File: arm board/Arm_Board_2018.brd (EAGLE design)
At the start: 100.3 x 64.8 mm, 190 parts, among them J1 RJ45KEYSTONE-942, J10 APP_2POS_CONFIGGENERAL_CONFIG, J11 APP_2POS_CONFIGGENERAL_CONFIG, J12 APP_2POS_CONFIGGENERAL_CONFIG, J13 APP_2POS_CONFIGGENERAL_CONFIG, J14 SL02, J15 SL02, J16 SL02, J2 JTAG_ARM_10PIN, J4 SL02, J5 APP_2POS_CONFIGGENERAL_CONFIG, J6 APP_2POS_CONFIGGENERAL_CONFIG, J7 APP_2POS_CONFIGGENERAL_CONFIG, J9 APP_2POS_CONFIGGENERAL_CONFIG, Q1 Q_IRF7437SMD, U1 TM4C1294NCPDT, U2 HX1198FNL, U3 SLVU2.8-4, Y1 NX3225GA, Y2 CRYATL_32K_SMD

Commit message: Switched wires to nets, corrected couple of naming errors
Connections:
- removed net MOTOR23_CURRENT_SENSOR: U$21.3
- removed net N$52: C44.1, C45.1, C46.1, C47.1
- removed net N$82: R61.1, R62.1, R63.1, R64.1, R65.1, R66.1
- removed net N$85: R55.2
- removed net N$86: R54.2
- net GND: now also C44.1, C45.1, C46.1, C47.1, R54.2, R55.2, R61.1, R62.1, R63.1, R64.1, R65.1, R66.1
- net MOTOR3_CURRENT_SENSOR: now also U$21.3

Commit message: Fixed remaining SCH issues, warnings, and missing parts
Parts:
- removed C50: 2.2uF, SparkFun-Passives:0603-CAP
- added C61, C63, C64, C65, C66, C67, C68: .1uF, SparkFun-Passives:0603-CAP
- added C62: 1nF, SparkFun-Passives:0603-CAP
- added C69, C70, C71, C72, C73, C74: 1uF, SparkFun-Passives:0603-CAP
- added C75: 2.2uF, SparkFun-Capacitors:1206
- added R59, R60, R67, R68, R69, R70: 1k, SparkFun-Passives:0402-RES
- C48, C49, C54: value (none) -> .1uF
- C51: device SparkFun-Passives:0603-CAP -> SparkFun-Capacitors:1206
- C53: value (none) -> 10uF
- moved C52 1187.1 mm to (64.8, -22.9)
- moved C53 1187.1 mm to (64.8, -52.1)
- moved C55 1187.1 mm to (64.8, -54.6)
- moved C56 1187.1 mm to (64.8, -57.1)
- moved C57 1187.1 mm to (64.8, -59.7)
- moved C58 1187.1 mm to (64.8, -62.2)
- moved C59 1187.1 mm to (64.8, -64.8)
- moved C60 1187.1 mm to (64.8, -67.3)
- moved POWER_12V 1187.1 mm to (132.1, 57.1)
- moved Q1 1187.1 mm to (74.9, -39.4)
- moved R51 1187.1 mm to (124.5, -19.1)
- moved R52 1187.1 mm to (120.7, -19.1)
- moved R53 1187.1 mm to (116.8, -19.1)
- moved R54 1187.1 mm to (113.0, -19.1)
- moved R55 1187.1 mm to (109.2, -19.1)
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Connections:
- new net N$12: R59.1, U$24.3
- new net N$13: R60.1, U$25.3
- new net N$20: R67.1, U$23.3
- new net N$32: R68.1, U$21.3
- new net N$38: R69.1, U$22.3
- new net N$44: R70.1, U$20.3
- net GND: now also C51.1, C61.2, C62.1, C63.1, C64.1, C65.1, C66.1, C67.1, C68.1, C69.2, C70.2, C71.1, C72.1, C73.1, C74.1, C75.2; no longer C50.2, C51.2
- net LOGIC_3.3V: now also C61.1, C63.2, C64.2, C65.2, C66.2, C67.2, C68.2, C75.1; no longer C50.1
- net MAINLINE_CURRENT_SENSOR: now also C62.2
- net MOTOR1_CURRENT_SENSOR: now also C74.2, R70.2; no longer U$20.3
- net MOTOR2_CURRENT_SENSOR: now also C73.2, R69.2; no longer U$22.3
- net MOTOR3_CURRENT_SENSOR: now also C72.2, R68.2; no longer U$21.3
- net MOTOR4_CURRENT_SENSOR: now also C71.2, R67.2; no longer U$23.3
- net MOTOR5_CURRENT_SENSOR: now also C69.1, R59.2; no longer U$24.3
- net MOTOR6_CURRENT_SENSOR: now also C70.1, R60.2; no longer U$25.3
- net VCC_12V: now also C51.2; no longer C51.1
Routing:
- net !RESET: track 80.8 -> 70.4 mm
- removed copper zone on layer 1, net +12V_ACT
- removed copper zone on layer 1, net +12V_LOGIC
- removed copper zone on layer 1, net +5V_ACT
- removed copper zone on layer 1, net +5V_LOGIC

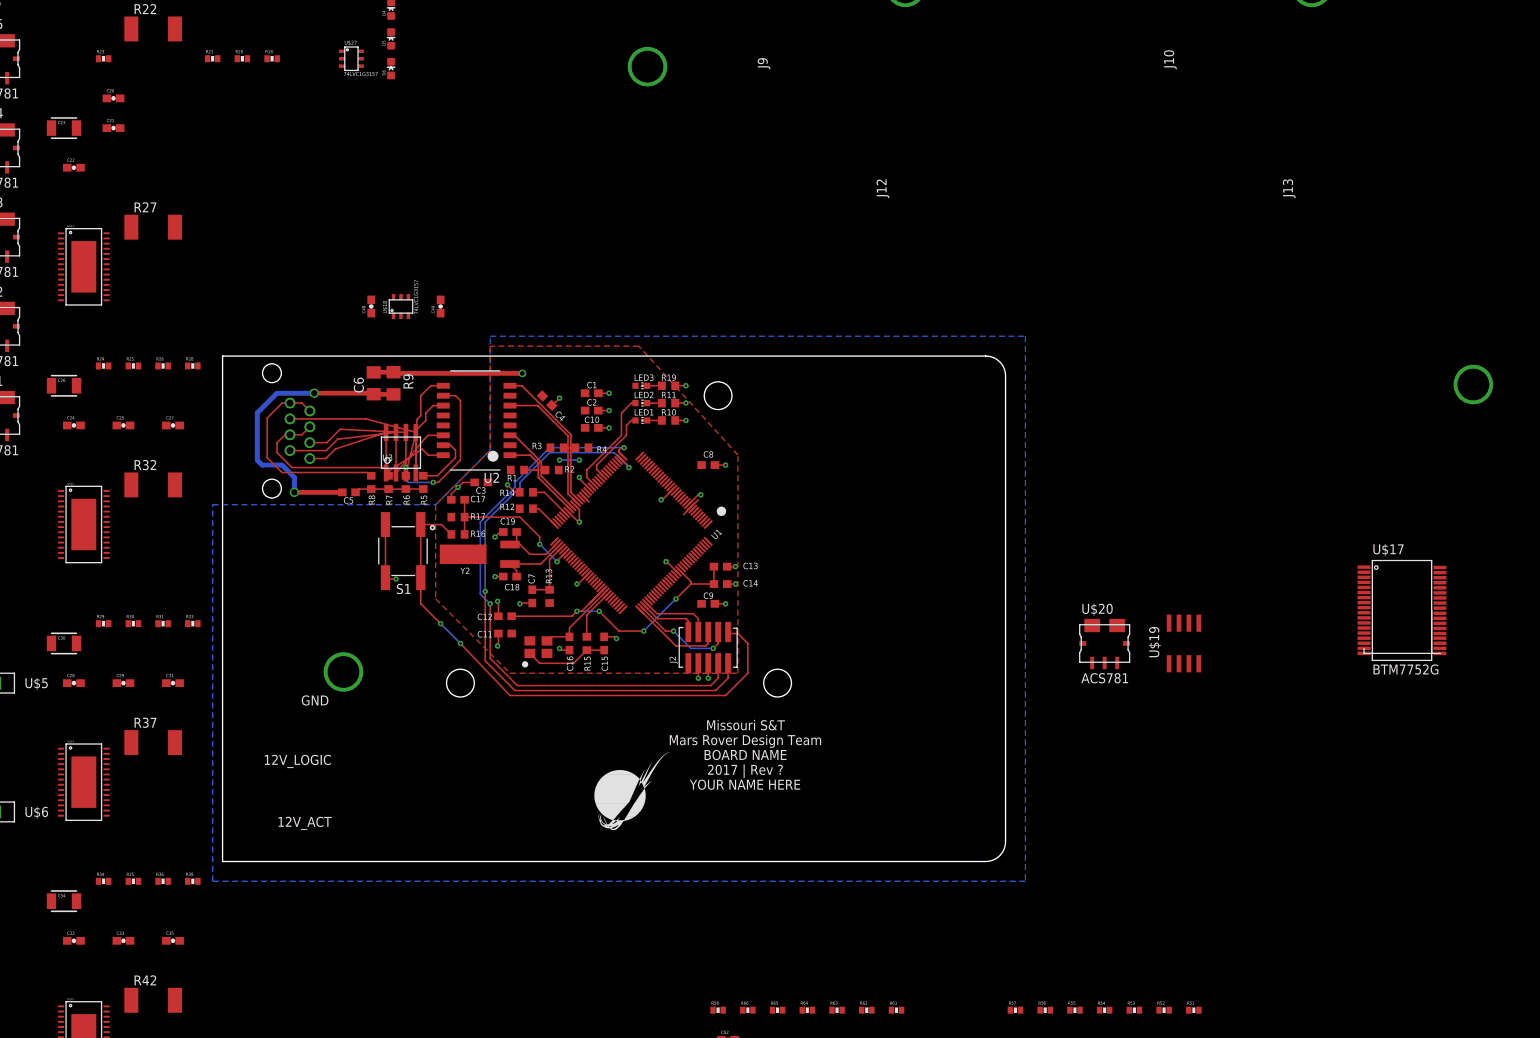
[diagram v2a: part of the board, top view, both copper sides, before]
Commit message: Changed +3V3 to LOGIC_3.3V
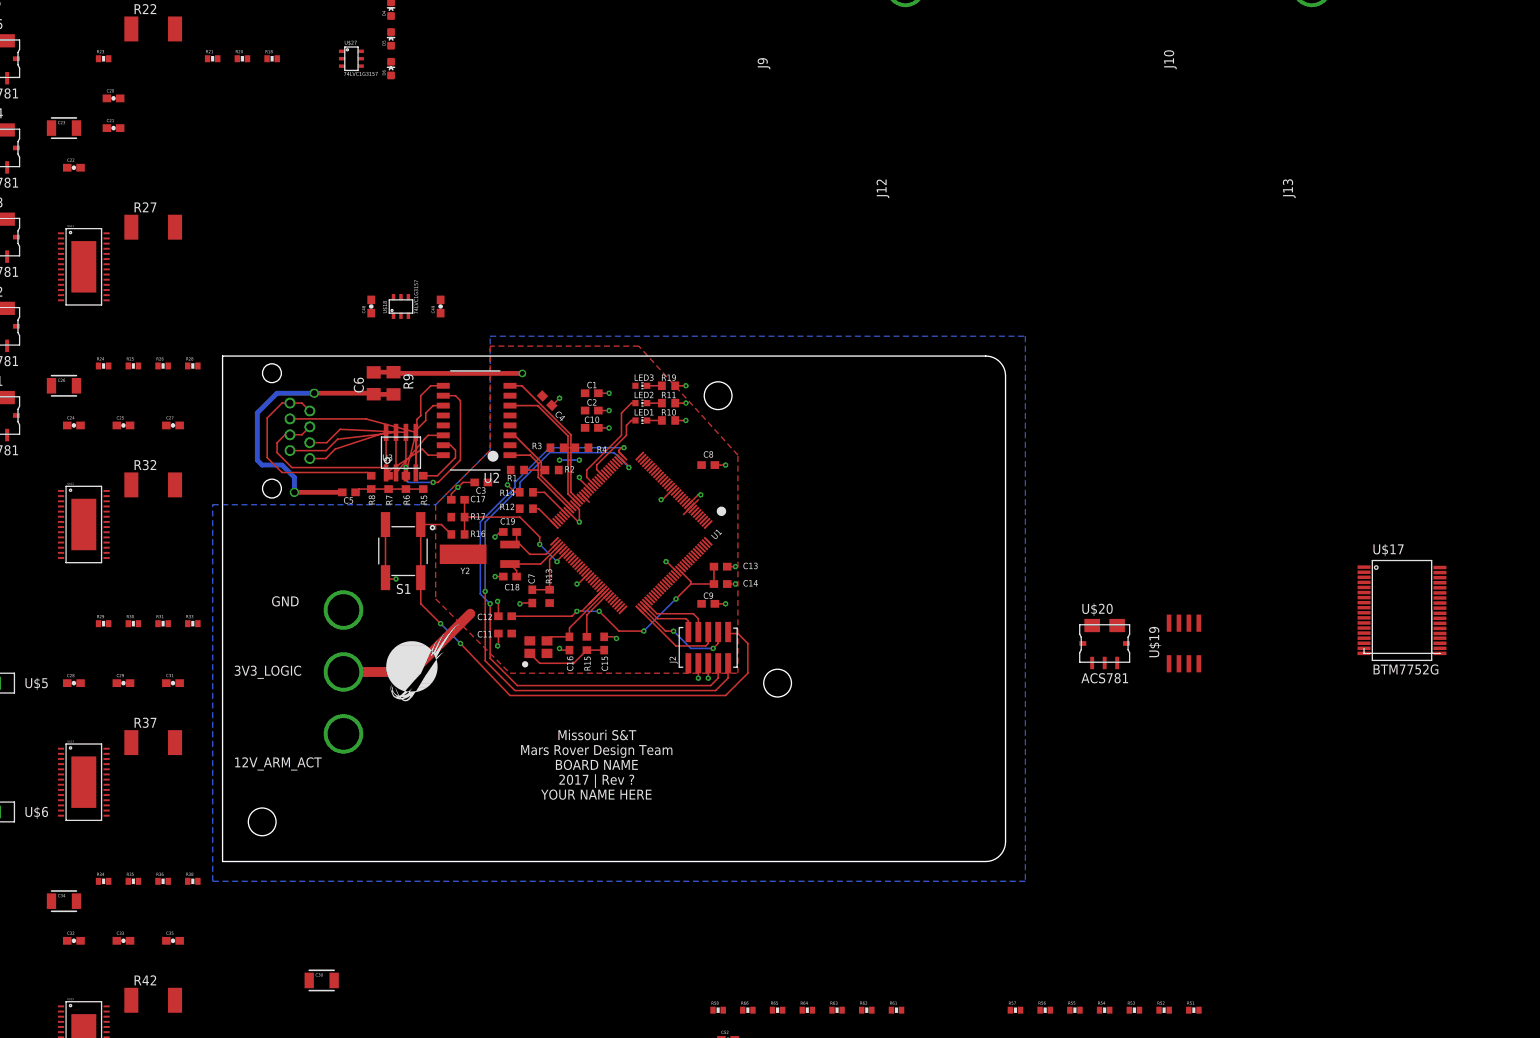
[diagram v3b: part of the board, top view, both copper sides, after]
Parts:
- moved POWER_12V 151.5 mm to (-12.7, 12.4)
- moved GND 84.4 mm to (-12.7, 28.3), turned to 0 degrees
- moved C30 54.4 mm to (12.7, -15.2)
- moved U$1 31.4 mm to (21.0, 19.7)
- moved U$3 31.0 mm to (5.08, 5.08)
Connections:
- removed net +3V3: C1.1, C10.1, C11.1, C2.1, C3.1, C4.1, C8.1, C9.1, J2.P1, LED3.A, R1.1, R12.2, R13.2, R17.1, R2.1, R3.1, R4.1, U1.P$101, U1.P$113, U1.P$122, U1.P$16, U1.P$26, U1.P$28, U1.P$39, U1.P$47, U1.P$51, U1.P$52, U1.P$69, U1.P$7, U1.P$79, U1.P$8, U1.P$9, U1.P$90, U2.P$2, U2.P$7
- net LOGIC_3.3V: now also C1.1, C10.1, C11.1, C2.1, C3.1, C4.1, C8.1, C9.1, J2.P1, LED3.A, R1.1, R12.2, R13.2, R17.1, R2.1, R3.1, R4.1, U1.P$101, U1.P$113, U1.P$122, U1.P$16, U1.P$26, U1.P$28, U1.P$39, U1.P$47, U1.P$51, U1.P$52, U1.P$69, U1.P$7, U1.P$79, U1.P$8, U1.P$9, U1.P$90, U2.P$2, U2.P$7
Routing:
- net LOGIC_3.3V: track 0.00 -> 25.8 mm, vias 0 -> 2
- net +3V3: track 6.46 -> 0.00 mm, vias 2 -> 0
- added copper zone on layer 1, net LOGIC_3.3V
- removed copper zone on layer 1, net +3V3
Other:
- board text added: "12V_ARM_ACT"
- board text added: "3V3_LOGIC"
- board text removed: "12V_ACT"
- board text removed: "12V_LOGIC"

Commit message: Revert "Changed +3V3 to LOGIC_3.3V"
This reverts commit afd64b7472180079d62c8d462dc00da2640ede11.
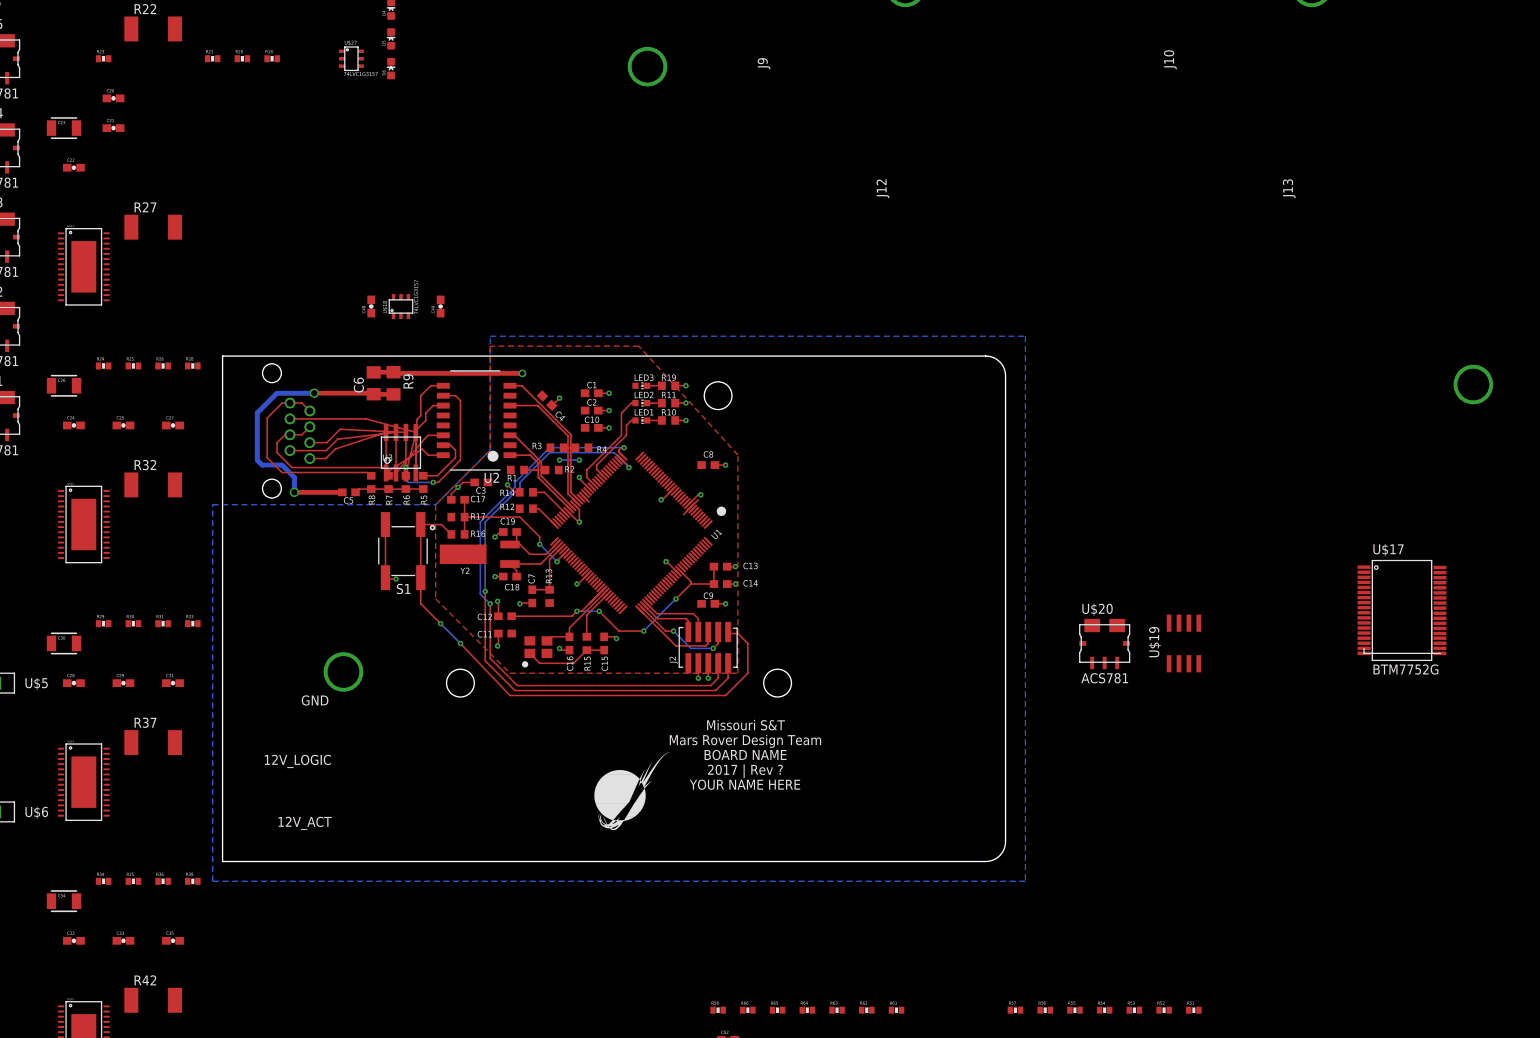
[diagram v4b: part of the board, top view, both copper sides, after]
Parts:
- moved POWER_12V 151.5 mm to (132.1, 57.1)
- moved GND 84.4 mm to (58.4, 73.7), turned to 90 degrees
- moved C30 54.4 mm to (-20.3, 27.9)
- moved U$1 31.4 mm to (47.6, 3.17)
- moved U$3 31.0 mm to (30.5, 22.9)
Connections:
- new net +3V3: C1.1, C10.1, C11.1, C2.1, C3.1, C4.1, C8.1, C9.1, J2.P1, LED3.A, R1.1, R12.2, R13.2, R17.1, R2.1, R3.1, R4.1, U1.P$101, U1.P$113, U1.P$122, U1.P$16, U1.P$26, U1.P$28, U1.P$39, U1.P$47, U1.P$51, U1.P$52, U1.P$69, U1.P$7, U1.P$79, U1.P$8, U1.P$9, U1.P$90, U2.P$2, U2.P$7
- net LOGIC_3.3V: no longer C1.1, C10.1, C11.1, C2.1, C3.1, C4.1, C8.1, C9.1, J2.P1, LED3.A, R1.1, R12.2, R13.2, R17.1, R2.1, R3.1, R4.1, U1.P$101, U1.P$113, U1.P$122, U1.P$16, U1.P$26, U1.P$28, U1.P$39, U1.P$47, U1.P$51, U1.P$52, U1.P$69, U1.P$7, U1.P$79, U1.P$8, U1.P$9, U1.P$90, U2.P$2, U2.P$7
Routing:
- net LOGIC_3.3V: track 25.8 -> 0.00 mm, vias 2 -> 0
- net +3V3: track 0.00 -> 6.46 mm, vias 0 -> 2
- added copper zone on layer 1, net +3V3
- removed copper zone on layer 1, net LOGIC_3.3V
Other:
- board text added: "12V_ACT"
- board text added: "12V_LOGIC"
- board text removed: "12V_ARM_ACT"
- board text removed: "3V3_LOGIC"

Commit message: Attached most of the powerlines
All major components put on the board. Most powerlines have been run.
Started to route a logic bus.
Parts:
- removed R60, R67, R68, R69, R70: 1k, SparkFun-Passives:0402-RES
- added C50: 2.2uF, SparkFun-Passives:0603-CAP
- added POWER_12V2: APPPP45_PCB_HORIZ_RIGHT, MRDT-Connectors:APP45_PCB_HORIZ_RIGHT
- added U$30: MOUNTING_HOLE#6, MRDT-Hardware:#6_SCREW
- C51: value 2.2uF -> 10nF; device SparkFun-Capacitors:1206 -> SparkFun-Passives:0603-CAP
- C61: value .1uF -> 2.2uF; device SparkFun-Passives:0603-CAP -> SparkFun-Passives:1206
- C62: value 1nF -> 2.2uF; device SparkFun-Passives:0603-CAP -> SparkFun-Passives:1206
- C63, C65, C67: value .1uF -> 0.1uF
- C64, C66, C68: value .1uF -> 10nF
- C69, C71, C73, C74: value 1uF -> 0.1uF
- C70, C72: value 1uF -> 10nF
- C75: value 2.2uF -> 1nF; device SparkFun-Capacitors:1206 -> SparkFun-Passives:0603-CAP
- R59: value 1k -> 1K
- U$21, U$22, U$23, U$24, U$25: value ACS781 -> ACS722LL; device MRDT-ICs:7-POWER_SMD_MODULE -> MRDT-ICs:SOIC8
- moved J16 455.0 mm to (-229.9, -38.1), turned to 0 degrees
- moved J15 434.6 mm to (-229.9, -21.6), turned to 0 degrees
- moved J14 414.7 mm to (-229.9, -5.08), turned to 0 degrees
- moved R54 409.4 mm to (-261.6, 146.1)
- moved R55 404.4 mm to (-261.6, 142.2)
- moved C62 348.6 mm to (-8.13, 261.6)
- moved C61 345.5 mm to (-3.05, 261.6)
- moved C51 340.0 mm to (-17.8, 206.5)
- moved C48 313.0 mm to (328.7, 25.4), turned to 0 degrees
- moved C49 305.7 mm to (328.7, 16.5), turned to 0 degrees
- moved C74 305.4 mm to (-17.8, 169.9)
- moved C73 303.9 mm to (-17.8, 173.0)
- moved R51 303.1 mm to (373.1, 154.2)
- moved R52 303.1 mm to (369.3, 154.2)
- moved R53 303.1 mm to (365.5, 154.2)
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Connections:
- removed net N$13: R60.1, U$25.3
- removed net N$14: C53.2, Q1.TAB, U$19.6, U$19.8, U$26.3, U$26.4
- removed net N$2: C56.2, R29.2, R30.2, U$12.12, U$12.13, U$12.17, U$12.23, U$12.24, U$12.25, U$12.26, U$12.27
- removed net N$26: C58.2, R34.2, R35.2, U$13.12, U$13.13, U$13.17, U$13.23, U$13.24, U$13.25, U$13.26, U$13.27
- removed net N$3: C55.2, R18.2, R20.2, U$14.12, U$14.13, U$14.17, U$14.23, U$14.24, U$14.25, U$14.26, U$14.27
- removed net N$4: C59.2, R39.2, R40.2, U$15.12, U$15.13, U$15.17, U$15.23, U$15.24, U$15.25, U$15.26, U$15.27
- removed net N$44: R70.1, U$20.3
- new net N$100: R59.2, U$20.3
- new net N$48: C53.2, Q1.TAB, U$19.6, U$19.8, U$20.6
- new net N$52: C65.2, U$21.6, U$21.8
- new net N$76: C64.2, U$21.7
- new net N$78: C67.2, U$22.6, U$22.8
- new net N$82: C66.2, U$22.7
- new net N$83: C69.2, U$24.6, U$24.8
- new net N$84: C68.2, U$24.7
- new net N$85: C71.2, U$26.6, U$26.8
- new net N$86: C70.2, U$26.7
- new net N$87: C73.2, U$25.6, U$25.8
- new net N$96: C72.2, U$25.7
- new net N$98: C63.2, U$23.6, U$23.8
- new net N$99: C51.2, U$23.7
- net 12VMOTOR_POWER: now also U$21.1, U$21.2, U$22.1, U$22.2, U$23.1, U$23.2, U$24.1, U$24.2, U$25.1, U$25.2, U$26.1, U$26.2; no longer U$20.5, U$21.5, U$22.5, U$23.5, U$24.5, U$25.5
- net GND: now also C50.2, C61.1, C74.2, U$20.4, U$20.7, U$21.5, U$22.5, U$23.5, U$24.5, U$25.5; no longer C51.1, C61.2, C63.1, C64.1, C65.1, C66.1, C67.1, C68.1, C69.2, C70.2, C71.1, C72.1, C73.1, C74.1, U$21.2, U$22.2, U$23.2, U$24.2, U$25.2
- net LOGIC_3.3V: now also C50.1, C63.1, C65.1, C67.1, C69.1, C71.1, C73.1, C74.1; no longer C61.1, C63.2, C64.2, C65.2, C66.2, C67.2, C68.2, C75.1, U$21.1, U$22.1, U$23.1, U$24.1, U$25.1, U$26.6, U$26.8
- net MAINLINE_CURRENT_SENSOR: now also C75.1, R59.1; no longer C62.2, U$26.7
- net MOTOR1_CURRENT_SENSOR: now also C64.1; no longer C74.2, R70.2
- net MOTOR1_POWER: now also U$21.3, U$21.4; no longer U$20.6
- net MOTOR2_CURRENT_SENSOR: now also C66.1; no longer C73.2, R69.2
- net MOTOR2_POWER: now also U$22.3, U$22.4; no longer U$22.6
- net MOTOR3_CURRENT_SENSOR: now also C51.1; no longer C72.2, R68.2
- net MOTOR3_POWER: now also U$23.3, U$23.4; no longer U$21.6
- net MOTOR4_CURRENT_SENSOR: now also C68.1; no longer C71.2, R67.2
- net MOTOR4_POWER: now also U$24.3, U$24.4; no longer U$23.6
- net MOTOR5_CURRENT_SENSOR: now also C72.1; no longer C69.1, R59.2
- net MOTOR5_POWER: now also U$25.3, U$25.4; no longer U$24.6
- net MOTOR6_CURRENT_SENSOR: no longer R60.2
- net MOTOR6_POWER: now also U$26.3, U$26.4; no longer U$25.6
- net N$1: now also C55.2, R18.2, R20.2, U$14.15, U$14.17, U$14.23, U$14.24, U$14.25, U$14.26, U$14.27; no longer C57.2, R24.2, R25.2, U$11.12, U$11.13, U$11.17, U$11.23, U$11.24, U$11.25, U$11.26, U$11.27
- net N$12: now also R20.1, R21.2, U$14.12, U$14.13; no longer R59.1, U$24.3
- net N$15: now also R35.1, R36.2, U$13.12, U$13.13; no longer R25.1, R26.2, U$11.15
- net N$20: now also C57.2, R24.2, R25.2, U$11.15, U$11.17, U$11.23, U$11.24, U$11.25, U$11.26, U$11.27; no longer R67.1, U$23.3
- net N$21: now also R45.1, R46.2, U$16.12, U$16.13; no longer R30.1, R31.2, U$12.15
- net N$27: now also R40.1, R41.2, U$15.12, U$15.13; no longer R35.1, R36.2, U$13.15
- net N$32: now also C59.2, R39.2, R40.2, U$15.15, U$15.17, U$15.23, U$15.24, U$15.25, U$15.26, U$15.27; no longer R68.1, U$21.3
- net N$33: now also C60.2, R44.2, R45.2, U$16.15, U$16.17, U$16.23, U$16.24, U$16.25, U$16.26, U$16.27; no longer R40.1, R41.2, U$15.15
- net N$38: now also C56.2, R29.2, R30.2, U$12.15, U$12.17, U$12.23, U$12.24, U$12.25, U$12.26, U$12.27; no longer R69.1, U$22.3
- net N$39: now also C58.2, R34.2, R35.2, U$13.15, U$13.17, U$13.23, U$13.24, U$13.25, U$13.26, U$13.27; no longer R45.1, R46.2, U$16.15
- net N$5: now also R30.1, R31.2, U$12.12, U$12.13; no longer C60.2, R44.2, R45.2, U$16.12, U$16.13, U$16.17, U$16.23, U$16.24, U$16.25, U$16.26, U$16.27
- net N$6: now also R25.1, R26.2, U$11.12, U$11.13; no longer R20.1, R21.2, U$14.15
- net VCC_12V: now also C61.2, C62.2, POWER_12V2.P$1, U$20.5; no longer C51.2, U$26.1, U$26.2
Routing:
- net GND: track 77.2 -> 239.1 mm, vias 30 -> 111
- net MOTOR1_2: track 0.00 -> 141.8 mm, vias 0 -> 3
- net MOTOR3_2: track 0.00 -> 125.2 mm, vias 0 -> 3
- net MOTOR1_POWER: track 0.00 -> 121.1 mm, vias 0 -> 4
- net MOTOR1_1: track 0.00 -> 110.9 mm, vias 0 -> 2
- net MOTOR3_POWER: track 0.00 -> 95.0 mm, vias 0 -> 1
- net MOTOR6_2: track 0.00 -> 94.8 mm, vias 0 -> 1
- net LOGIC_3.3V: track 0.00 -> 90.4 mm, vias 0 -> 1
- net MOTOR4_2: track 0.00 -> 84.1 mm, vias 0 -> 2
- net MOTOR6_1: track 0.00 -> 81.3 mm, vias 0 -> 1
- net MOTOR7_2: track 0.00 -> 74.0 mm, vias 0 -> 1
- net MOTOR4_1: track 0.00 -> 73.1 mm, vias 0 -> 1
- net MOTOR5_POWER: track 0.00 -> 65.7 mm, vias 0 -> 3
- net MOTOR7_1: track 0.00 -> 64.7 mm, vias 0 -> 1
- net MOTOR2_POWER: track 0.00 -> 63.4 mm, vias 0 -> 1
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- added copper zone on layer 1, net 12VMOTOR_POWER
- added copper zone on layer 2, net 12VMOTOR_POWER
- added copper zone on layer 1, net GND
- added copper zone on layer 1, net MOTOR1_1
- added copper zone on layer 1, net MOTOR1_2
- added copper zone on layer 1, net MOTOR1_POWER
- added copper zone on layer 1, net MOTOR2_2
- added copper zone on layer 1, net MOTOR2_POWER
- added copper zone on layer 1, net MOTOR3_1
- added copper zone on layer 1, net MOTOR3_2
- added copper zone on layer 1, net MOTOR3_POWER
- added copper zone on layer 1, net MOTOR4_POWER
- added copper zone on layer 1, net MOTOR5_POWER
- added copper zone on layer 1, net MOTOR6_2
- added copper zone on layer 1, net MOTOR7_2
- added copper zone on layer 1, net MOTOR8_2
- added copper zone on layer 1, net N$1
- added copper zone on layer 1, net N$20
- added copper zone on layer 1, net N$32
- added copper zone on layer 1, net N$33
- added copper zone on layer 1, net N$38
- added copper zone on layer 1, net N$39
- added copper zone on layer 1, net N$48
- added copper zone on layer 2, net N$48
- added copper zone on layer 1, net VCC_12V
- added copper zone on layer 2, net VCC_12V
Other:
- board size 100.3 x 64.8 mm -> 236.5 x 96.8 mm
- board text added: "Missouri S&T Mars Rover Design Team BOARD NAME 2017 | Rev 1 David Strickland"
- board text removed: "Missouri S&T Mars Rover Design Team BOARD NAME 2017 | Rev ? YOUR NAME HERE"
